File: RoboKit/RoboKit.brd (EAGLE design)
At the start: 134 x 82 mm, 32 parts, among them CON1 XT30UPB-M, CON2 XT30UPB-M, P1 B6B-PH-K, P2 B6B-PH-K, U1 SSM6J808R, X3 JST-XH-02-PIN-LONG-PAD, X4 JST-XH-02-PIN-LONG-PAD, X5 JST-XH-04-PIN-LONG-PAD, X6 JST-XH-04-PIN-LONG-PAD, X7 JST-XH-10-PIN-LONG-PAD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

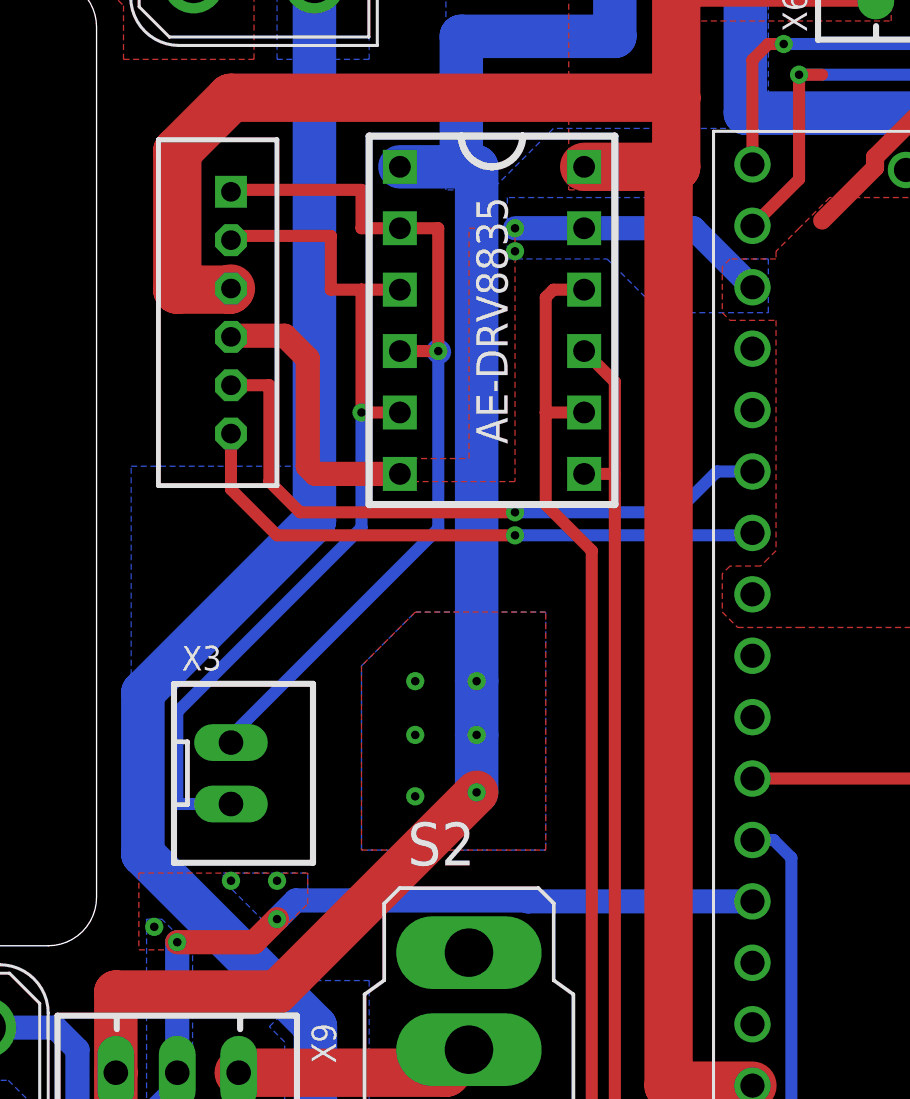
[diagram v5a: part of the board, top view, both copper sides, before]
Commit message: ビアの位置を修正
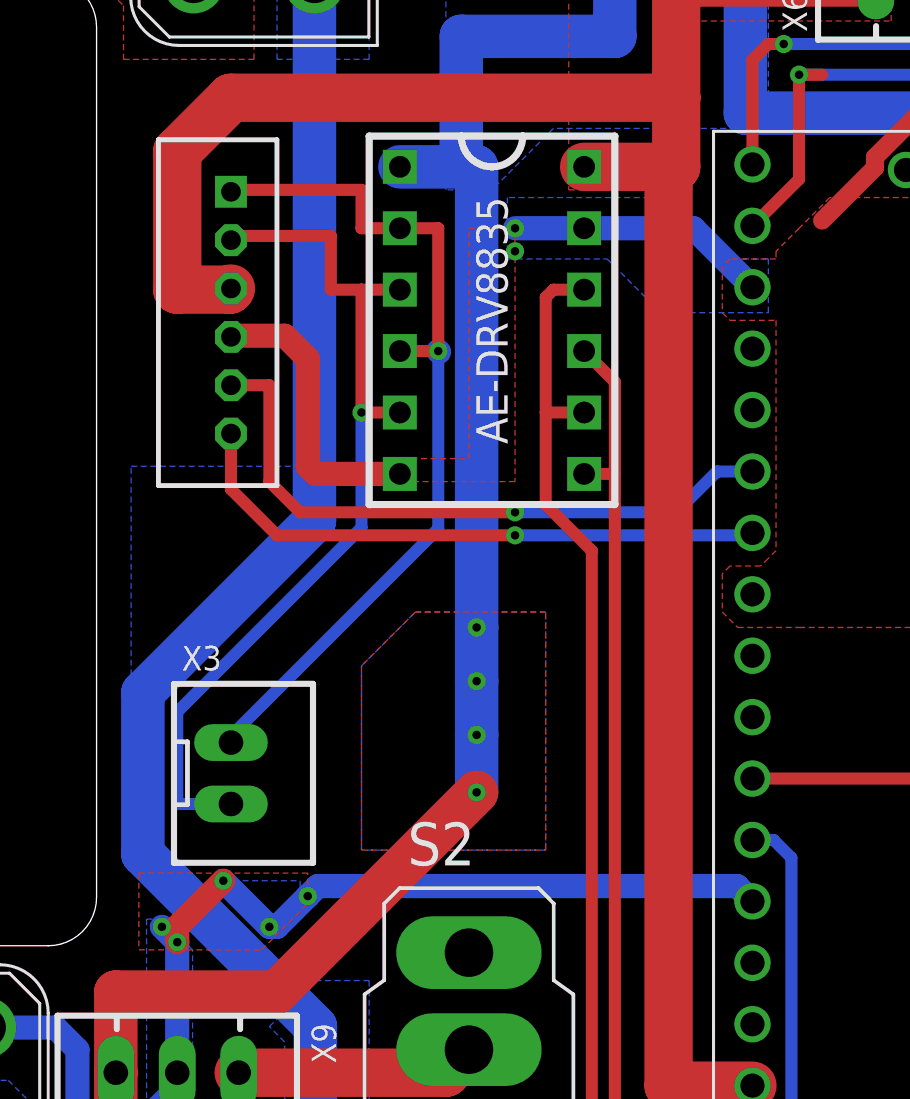
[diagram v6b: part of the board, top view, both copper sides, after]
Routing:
- net GND: track 190.0 -> 193.4 mm, vias 8 -> 11
- net VOUT: vias 7 -> 8
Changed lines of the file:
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@@
 <via x="93.345" y="43.815" extent="1-16" drill="0.35"/>
 <wire x1="93.345" y1="43.815" x2="87.63" y2="43.815" width="1" layer="16"/>
-<wire x1="57.1275" y1="38.835" x2="47.83910625" y2="38.835" width="1" layer="16"/>
-<wire x1="47.83910625" y1="38.835" x2="47.80105625" y2="38.87305" width="1" layer="16"/>
-<wire x1="47.80105625" y1="38.87305" x2="38.23805" y2="38.87305" width="1" layer="16"/>
-<wire x1="38.23805" y1="38.87305" x2="37.465" y2="38.1" width="1" layer="16"/>
-<via x="37.465" y="38.1" extent="1-16" drill="0.35"/>
-<wire x1="37.465" y1="38.1" x2="36.5125" y2="37.1475" width="1" layer="1"/>
-<wire x1="36.5125" y1="37.1475" x2="33.3375" y2="37.1475" width="1" layer="1"/>
+<wire x1="57.1275" y1="38.835" x2="56.4925" y2="39.47" width="1" layer="16"/>
+<wire x1="56.4925" y1="39.47" x2="39.1525" y2="39.47" width="1" layer="16"/>
 <via x="33.3375" y="37.1475" extent="1-16" drill="0.35"/>
 <wire x1="33.3375" y1="31.75" x2="33.3375" y2="37.1475" width="1" layer="16"/>
@@
 </polygon>
 <polygon width="0.5" layer="16">
-<vertex x="37.465" y="37.465"/>
-<vertex x="35.2425" y="39.6875"/>
-<vertex x="35.2425" y="40.005"/>
-<vertex x="38.735" y="40.005"/>
-<vertex x="38.735" y="38.735"/>
-</polygon>
-<polygon width="0.5" layer="16">
 <vertex x="46.99" y="65.405"/>
 <vertex x="51.1175" y="65.405"/>
@@
 <vertex x="46.99" y="67.945"/>
 </polygon>
+<wire x1="39.1525" y1="39.47" x2="38.735" y2="39.0525" width="1" layer="16"/>
+<wire x1="38.735" y1="39.0525" x2="37.465" y2="37.7825" width="1" layer="16"/>
+<wire x1="37.465" y1="37.7825" x2="37.1475" y2="37.7825" width="1" layer="16"/>
+<wire x1="37.1475" y1="37.7825" x2="35.2425" y2="39.6875" width="1" layer="16"/>
+<via x="35.2425" y="39.6875" extent="1-16" drill="0.35"/>
+<via x="37.1475" y="37.7825" extent="1-16" drill="0.35"/>
+<via x="38.735" y="39.0525" extent="1-16" drill="0.35"/>
+<wire x1="33.3375" y1="37.7825" x2="33.3375" y2="37.1475" width="1" layer="1"/>
+<wire x1="35.2425" y1="39.6875" x2="33.3375" y2="37.7825" width="1" layer="1"/>
+<wire x1="33.3375" y1="37.1475" x2="32.7025" y2="37.7825" width="1" layer="16"/>
+<via x="32.7025" y="37.7825" extent="1-16" drill="0.35"/>
+<polygon width="1" layer="16">
+<vertex x="38.4175" y="39.6875"/>
+<vertex x="38.4175" y="38.735"/>
+<vertex x="37.465" y="37.7825"/>
+<vertex x="37.1475" y="37.7825"/>
+<vertex x="35.2425" y="39.6875"/>
+</polygon>
 <wire x1="74.9075" y1="26.135" x2="74.9075" y2="38.835" width="0" layer="19" extent="1-1"/>
 <wire x1="74.9075" y1="51.535" x2="74.9075" y2="38.835" width="0" layer="19" extent="1-1"/>
 <wire x1="84.455" y1="56.515" x2="74.9075" y2="51.535" width="0" layer="19" extent="1-1"/>
 <wire x1="60.0075" y1="66.9925" x2="74.9075" y2="64.235" width="0" layer="19" extent="1-1"/>
+<wire x1="42.545" y1="56.515" x2="47.3075" y2="66.675" width="0" layer="19" extent="1-1"/>
 <wire x1="57.1275" y1="38.835" x2="57.1275" y2="51.535" width="0" layer="19" extent="1-1"/>
 <wire x1="18.0975" y1="33.435" x2="17.4625" y2="33.02" width="0" layer="19" extent="1-1"/>
@@
 <wire x1="51.435" y1="74.6125" x2="45.085" y2="74.6125" width="1.8" layer="16"/>
 <wire x1="45.085" y1="74.6125" x2="45.085" y2="69.215" width="1.8" layer="16"/>
-<wire x1="45.72" y1="69.215" x2="45.72" y2="47.9425" width="1.8" layer="16"/>
+<wire x1="45.72" y1="69.215" x2="45.72" y2="50.165" width="1.8" layer="16"/>
+<wire x1="45.72" y1="50.165" x2="45.72" y2="47.9425" width="1.8" layer="16"/>
 <wire x1="45.72" y1="47.9425" x2="45.72" y2="45.72" width="1.8" layer="16"/>
 <wire x1="45.72" y1="45.72" x2="45.72" y2="43.34455" width="1.8" layer="16"/>
@@
 <vertex x="83.185" y="72.39"/>
 </polygon>
+<via x="45.72" y="50.165" extent="1-16" drill="0.35"/>
 </signal>
 <signal name="N$2">
@@
 <via x="94.9325" y="43.815" extent="1-16" drill="0.35"/>
 </signal>
-<signal name="N$12">
-<via x="32.385" y="37.7825" extent="1-16" drill="0.35"/>
-</signal>
-<signal name="N$13">
-<via x="37.465" y="39.6875" extent="1-16" drill="0.35"/>
-</signal>
-<signal name="N$14">
-<via x="35.56" y="39.6875" extent="1-16" drill="0.35"/>
-</signal>
-<signal name="N$8">
-<via x="43.18" y="43.18" extent="1-16" drill="0.35"/>
-</signal>
-<signal name="N$9">
-<via x="43.18" y="45.72" extent="1-16" drill="0.35"/>
-</signal>
-<signal name="N$10">
-<via x="43.18" y="47.9425" extent="1-16" drill="0.35"/>
-</signal>
 <signal name="N$15">

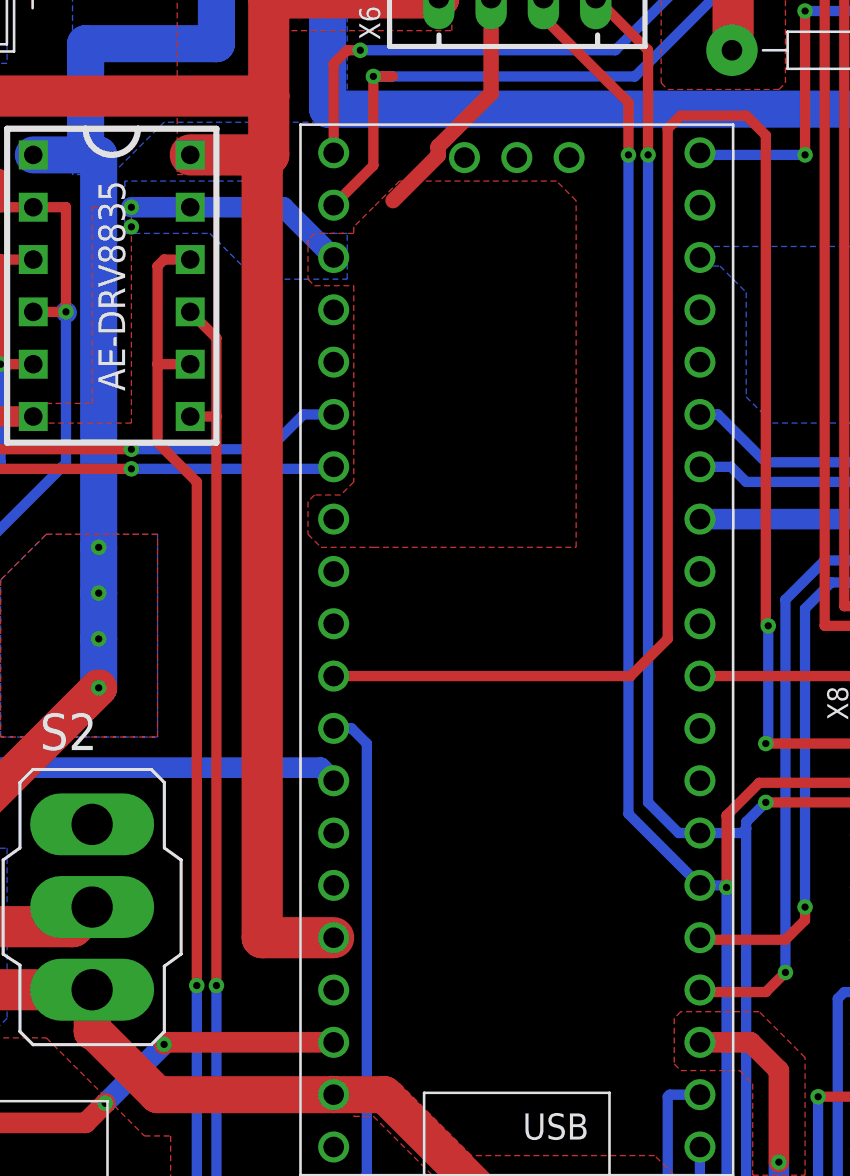
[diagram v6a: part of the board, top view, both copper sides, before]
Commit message: Air wireを修正
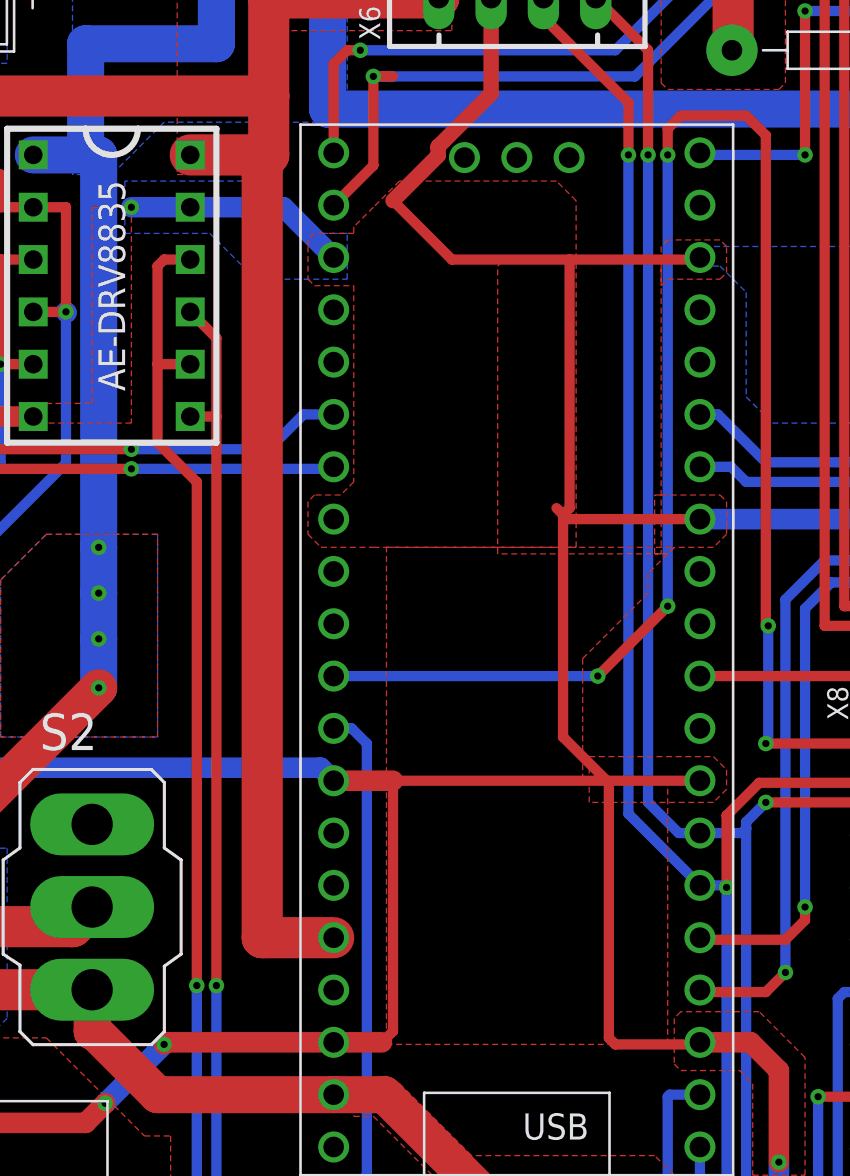
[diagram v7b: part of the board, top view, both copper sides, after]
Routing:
- net GND: track 193.4 -> 293.2 mm
- net Y-COM: track 116.3 -> 115.3 mm, vias 6 -> 9
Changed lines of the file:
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@@
 <vertex x="35.2425" y="39.6875"/>
 </polygon>
-<wire x1="74.9075" y1="26.135" x2="74.9075" y2="38.835" width="0" layer="19" extent="1-1"/>
-<wire x1="74.9075" y1="51.535" x2="74.9075" y2="38.835" width="0" layer="19" extent="1-1"/>
-<wire x1="84.455" y1="56.515" x2="74.9075" y2="51.535" width="0" layer="19" extent="1-1"/>
-<wire x1="60.0075" y1="66.9925" x2="74.9075" y2="64.235" width="0" layer="19" extent="1-1"/>
-<wire x1="42.545" y1="56.515" x2="47.3075" y2="66.675" width="0" layer="19" extent="1-1"/>
-<wire x1="57.1275" y1="38.835" x2="57.1275" y2="51.535" width="0" layer="19" extent="1-1"/>
-<wire x1="18.0975" y1="33.435" x2="17.4625" y2="33.02" width="0" layer="19" extent="1-1"/>
-<wire x1="35.8775" y1="22.225" x2="33.3375" y2="31.75" width="0" layer="19" extent="1-1"/>
+<wire x1="60.0075" y1="66.9925" x2="62.865" y2="64.135" width="0.5" layer="1"/>
+<wire x1="74.8075" y1="64.135" x2="74.9075" y2="64.235" width="0.5" layer="1"/>
+<wire x1="62.865" y1="64.135" x2="68.58" y2="64.135" width="0.5" layer="1"/>
+<wire x1="68.58" y1="64.135" x2="74.8075" y2="64.135" width="0.5" layer="1"/>
+<wire x1="68.58" y1="64.135" x2="68.58" y2="52.07" width="0.5" layer="1"/>
+<wire x1="68.58" y1="52.07" x2="68.2625" y2="51.7525" width="0.5" layer="1"/>
+<wire x1="74.9075" y1="51.535" x2="68.48" y2="51.535" width="0.5" layer="1"/>
+<wire x1="68.48" y1="51.535" x2="68.2625" y2="51.7525" width="0.5" layer="1"/>
+<wire x1="68.2625" y1="51.7525" x2="67.945" y2="52.07" width="0.5" layer="1"/>
+<wire x1="74.9075" y1="38.835" x2="70.385" y2="38.835" width="0.5" layer="1"/>
+<wire x1="70.385" y1="38.835" x2="68.2625" y2="40.9575" width="0.5" layer="1"/>
+<wire x1="68.2625" y1="40.9575" x2="68.2625" y2="51.7525" width="0.5" layer="1"/>
+<wire x1="57.1275" y1="38.835" x2="60.0075" y2="38.835" width="1" layer="1"/>
+<wire x1="60.0075" y1="38.835" x2="70.385" y2="38.835" width="0.5" layer="1"/>
+<wire x1="70.385" y1="38.835" x2="70.485" y2="38.735" width="0.5" layer="1"/>
+<wire x1="70.485" y1="38.735" x2="70.485" y2="26.3525" width="0.5" layer="1"/>
+<wire x1="70.485" y1="26.3525" x2="70.8025" y2="26.035" width="0.5" layer="1"/>
+<wire x1="74.8075" y1="26.035" x2="74.9075" y2="26.135" width="0.5" layer="1"/>
+<wire x1="70.8025" y1="26.035" x2="74.8075" y2="26.035" width="0.5" layer="1"/>
+<polygon width="0.5" layer="1">
+<vertex x="65.405" y="64.135"/>
+<vertex x="73.025" y="64.135"/>
+<vertex x="73.025" y="51.435"/>
+<vertex x="73.025" y="49.8475"/>
+<vertex x="65.0875" y="49.8475"/>
+<vertex x="65.0875" y="63.8175"/>
+</polygon>
+<polygon width="0.5" layer="1">
+<vertex x="73.025" y="52.705"/>
+<vertex x="75.8825" y="52.705"/>
+<vertex x="76.2" y="52.3875"/>
+<vertex x="76.2" y="51.1175"/>
+<vertex x="76.2" y="50.8"/>
+<vertex x="75.8825" y="50.4825"/>
+<vertex x="75.565" y="50.165"/>
+<vertex x="73.66" y="50.165"/>
+<vertex x="73.3425" y="49.8475"/>
+<vertex x="72.7075" y="49.8475"/>
+<vertex x="72.7075" y="52.705"/>
+</polygon>
+<polygon width="0.5" layer="1">
+<vertex x="73.025" y="62.865"/>
+<vertex x="73.3425" y="63.1825"/>
+<vertex x="75.8825" y="63.1825"/>
+<vertex x="76.2" y="63.5"/>
+<vertex x="76.2" y="64.77"/>
+<vertex x="75.8825" y="65.0875"/>
+<vertex x="73.3425" y="65.0875"/>
+<vertex x="73.025" y="64.77"/>
+</polygon>
+<polygon width="0.5" layer="1">
+<vertex x="68.58" y="50.165"/>
+<vertex x="73.66" y="50.165"/>
+<vertex x="72.39" y="48.895"/>
+<vertex x="72.39" y="47.9425"/>
+<vertex x="69.215" y="44.7675"/>
+<vertex x="69.215" y="38.735"/>
+<vertex x="59.69" y="38.735"/>
+<vertex x="59.69" y="50.165"/>
+</polygon>
+<polygon width="0.5" layer="1">
+<vertex x="69.5325" y="40.005"/>
+<vertex x="75.565" y="40.005"/>
+<vertex x="76.2" y="39.37"/>
+<vertex x="76.2" y="38.4175"/>
+<vertex x="75.565" y="37.7825"/>
+<vertex x="69.5325" y="37.7825"/>
+</polygon>
+<wire x1="57.1275" y1="26.135" x2="59.4725" y2="26.135" width="1" layer="1"/>
+<wire x1="60.0075" y1="26.67" x2="60.0075" y2="38.835" width="0.5" layer="1"/>
+<wire x1="59.4725" y1="26.135" x2="60.0075" y2="26.67" width="0.5" layer="1"/>
+<polygon width="0.5" layer="1">
+<vertex x="59.69" y="38.735"/>
+<vertex x="59.69" y="26.035"/>
+<vertex x="73.3425" y="26.035"/>
+<vertex x="73.3425" y="38.735"/>
+</polygon>
+<wire x1="17.4625" y1="33.02" x2="18.0975" y2="33.435" width="0" layer="19" extent="1-1"/>
 </signal>
 <signal name="IO3">
@@
 <contactref element="TC4052DP" pad="3"/>
 <contactref element="U$1" pad="31"/>
-<wire x1="57.1275" y1="43.915" x2="71.5375" y2="43.915" width="0.5" layer="1"/>
-<wire x1="73.3425" y1="45.72" x2="71.5375" y2="43.915" width="0.5" layer="1"/>
+<wire x1="57.1275" y1="43.915" x2="69.95" y2="43.915" width="0.5" layer="16"/>
+<wire x1="73.3425" y1="47.3075" x2="69.95" y2="43.915" width="0.5" layer="1"/>
 <via x="78.2226" y="46.355" extent="1-16" drill="0.35"/>
 <wire x1="78.105" y1="40.64" x2="78.2226" y2="40.7576" width="0.5" layer="16"/>
@@
 <wire x1="91.1225" y1="23.495" x2="95.885" y2="23.495" width="0.5" layer="1"/>
 <wire x1="73.3425" y1="70.485" x2="73.9775" y2="71.12" width="0.5" layer="1"/>
-<wire x1="73.3425" y1="70.485" x2="73.3425" y2="45.72" width="0.5" layer="1"/>
+<wire x1="73.3425" y1="70.485" x2="73.3425" y2="69.215" width="0.5" layer="1"/>
+<wire x1="73.3425" y1="69.215" x2="73.3425" y2="47.3075" width="0.5" layer="16"/>
 <wire x1="95.5675" y1="40.64" x2="87.9475" y2="40.64" width="0.5" layer="16"/>
 <wire x1="95.885" y1="40.3225" x2="95.5675" y2="40.64" width="0.5" layer="16"/>
@@
 <wire x1="78.105" y1="46.4726" x2="78.2226" y2="46.355" width="0.5" layer="1"/>
 <wire x1="78.105" y1="70.1675" x2="78.105" y2="46.4726" width="0.5" layer="1"/>
+<via x="73.3425" y="69.215" extent="1-16" drill="0.35"/>
+<via x="73.3425" y="47.3075" extent="1-16" drill="0.35"/>
+<via x="69.95" y="43.915" extent="1-16" drill="0.35"/>
 </signal>
 <signal name="3Y">
@@
 <via x="94.9325" y="43.815" extent="1-16" drill="0.35"/>
 </signal>
-<signal name="N$15">
-<via x="47.3075" y="65.7225" extent="1-16" drill="0.35"/>
-</signal>
 </signals>
